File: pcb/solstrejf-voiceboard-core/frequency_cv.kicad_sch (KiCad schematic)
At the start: 0 parts

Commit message: Inital draft of the voice board power supplys and core.
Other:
- title: (none) -> Frequency Control Voltage Summing Amplifier
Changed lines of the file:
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@@
 	(generator_version "8.0")
 	(paper "A4")
+	(title_block
+		(title "Frequency Control Voltage Summing Amplifier")
+		(date "2024-08-24")
+		(rev "1.0")
+	)
 )

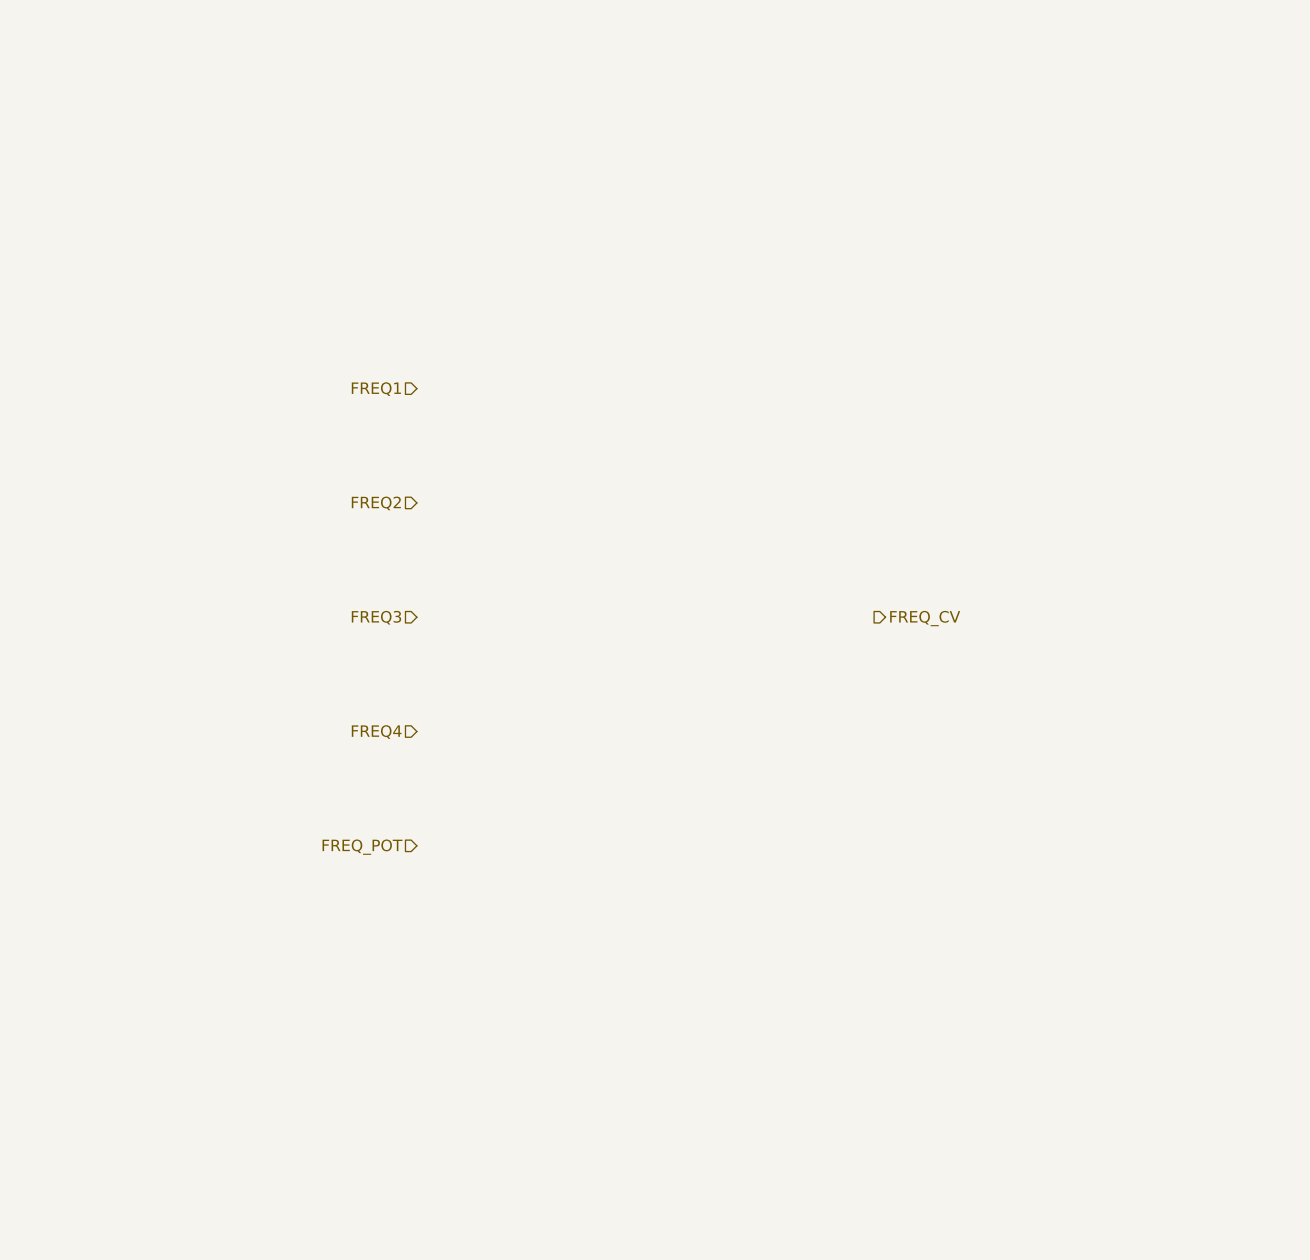
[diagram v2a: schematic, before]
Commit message: created schematic for CV circuits: PAN, VCA, and FREQ. Created a new symbol for the ONESHOT envelope generator
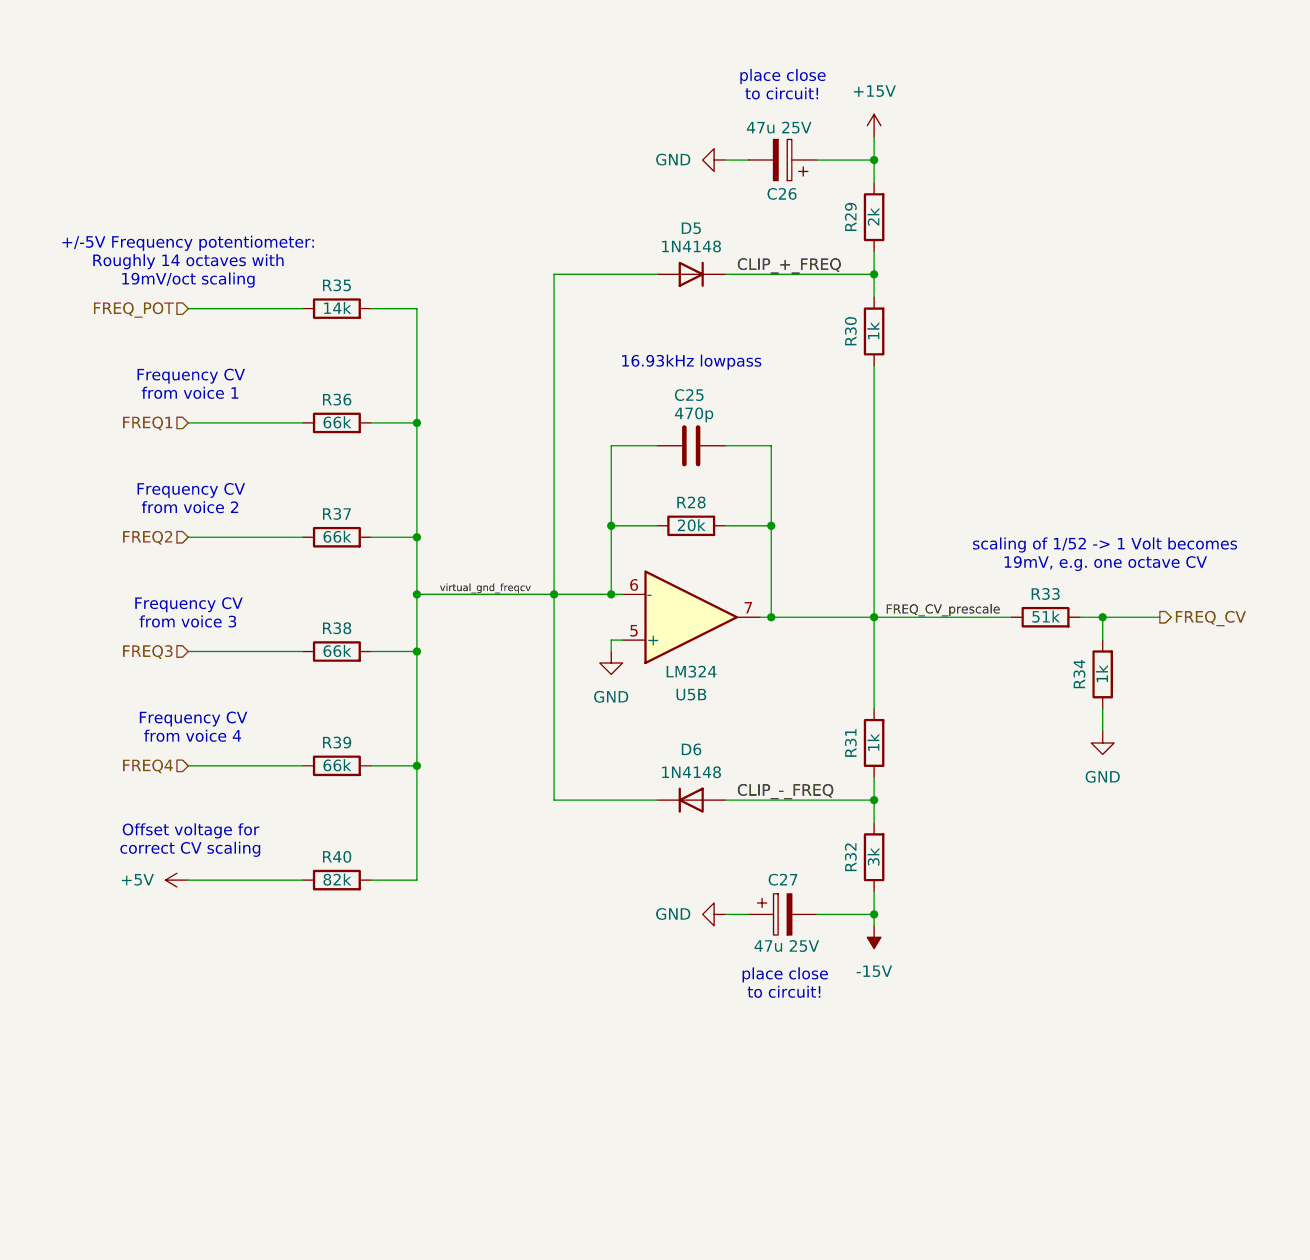
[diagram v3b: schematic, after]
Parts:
- added C25: 470p, Capacitor_THT:C_Disc_D5.0mm_W2.5mm_P5.00mm, symbol Device:C
- added C26, C27: 47u 25V, Capacitor_THT:CP_Radial_D5.0mm_P2.50mm, symbol Device:C_Polarized
- added D5, D6: 1N4148, Diode_THT:D_DO-35_SOD27_P7.62mm_Horizontal, symbol Diode:1N4148
- added R28: 20k, Resistor_THT:R_Axial_DIN0207_L6.3mm_D2.5mm_P10.16mm_Horizontal, symbol Device:R
- added R29: 2k, Resistor_THT:R_Axial_DIN0207_L6.3mm_D2.5mm_P10.16mm_Horizontal, symbol Device:R
- added R30, R31, R34: 1k, Resistor_THT:R_Axial_DIN0207_L6.3mm_D2.5mm_P10.16mm_Horizontal, symbol Device:R
- added R32: 3k, Resistor_THT:R_Axial_DIN0207_L6.3mm_D2.5mm_P10.16mm_Horizontal, symbol Device:R
- added R33: 51k, Resistor_THT:R_Axial_DIN0207_L6.3mm_D2.5mm_P10.16mm_Horizontal, symbol Device:R
- added R35: 14k, Resistor_THT:R_Axial_DIN0207_L6.3mm_D2.5mm_P10.16mm_Horizontal, symbol Device:R
- added R36, R37, R38, R39: 66k, Resistor_THT:R_Axial_DIN0207_L6.3mm_D2.5mm_P10.16mm_Horizontal, symbol Device:R
- added R40: 82k, Resistor_THT:R_Axial_DIN0207_L6.3mm_D2.5mm_P10.16mm_Horizontal, symbol Device:R
- added U5: LM324, Package_DIP:DIP-14_W7.62mm, symbol Amplifier_Operational:LM324
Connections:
- net FREQ1: now also R36.1
- net FREQ2: now also R37.1
- net FREQ3: now also R38.1
- net FREQ4: now also R39.1
- net FREQ_CV: now also R33.2, R34.2
- net FREQ_POT: now also R35.1
- new net +15V: C26.1, R29.2
- new net +5V: R40.1
- new net -15V: C27.2, R32.1
- new net CLIP_+_FREQ: D5.1 (K), R29.1, R30.2
- new net CLIP_-_FREQ: D6.2 (A), R31.1, R32.2
- new net FREQ_CV_prescale: C25.2, R28.2, R30.1, R31.2, R33.1, U5.7
- new net GND: C26.2, C27.1, R34.1, U5.5 (+)
- new net virtual_gnd_freqcv: C25.1, D5.2 (A), D6.1 (K), R28.1, R35.2, R36.2, R37.2, R38.2, R39.2, R40.2, U5.6 (-)
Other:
- note added: "+/-5V Frequency potentiometer: Roughly 14 octaves with 19mV/oct scaling"
- note added: "16.93kHz lowpass"
- note added: "Frequency CV from voice 1"
- note added: "Frequency CV from voice 2"
- note added: "Frequency CV from voice 3"
- note added: "Frequency CV from voice 4"
- note added: "Offset voltage for correct CV scaling"
- note added: "place close to circuit!"
- note added: "scaling of 1/52 -> 1 Volt becomes 19mV, e.g. one octave CV"

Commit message: Updated frequency CV summer circuit to use +/-12V local regulator instead of +/15V. Updated LTspice, notebooks, and KiCad project
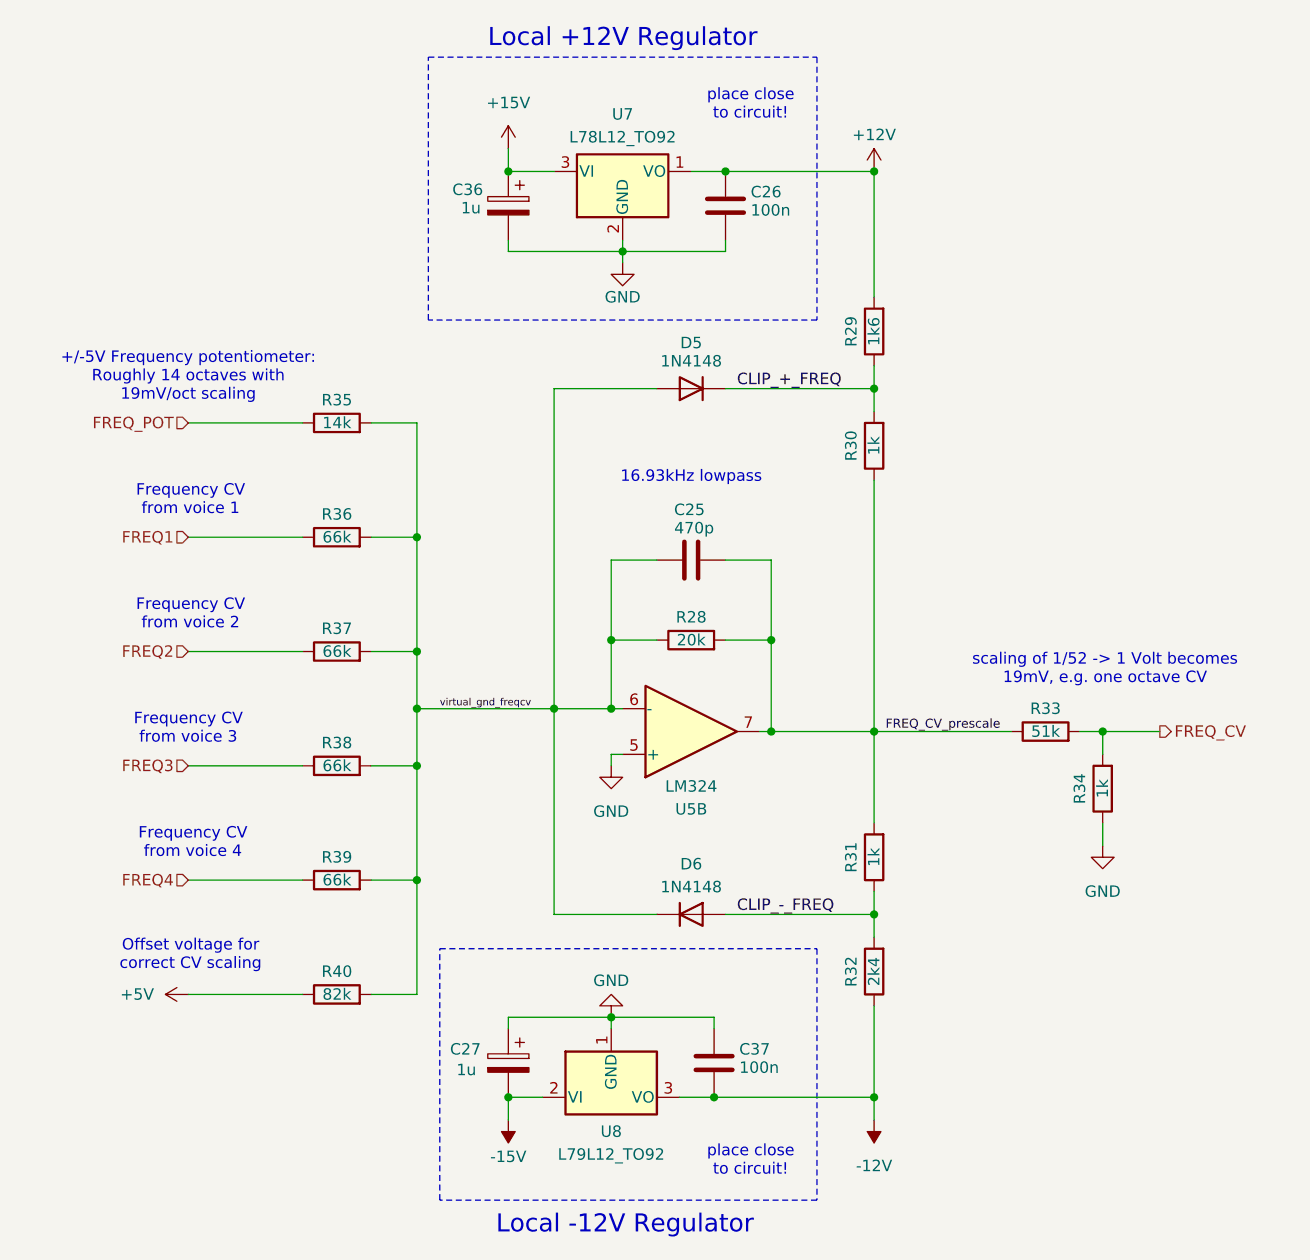
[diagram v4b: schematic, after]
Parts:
- removed C26: 47u 25V, Capacitor_THT:CP_Radial_D5.0mm_P2.50mm, symbol Device:C_Polarized
- added C26, C37: 100n, Capacitor_THT:C_Disc_D5.0mm_W2.5mm_P5.00mm, symbol Device:C
- added C36: 1u, Capacitor_THT:CP_Radial_D5.0mm_P2.50mm, symbol Device:C_Polarized
- added U7: L78L12_TO92, Package_TO_SOT_THT:TO-92_Inline, symbol Regulator_Linear:L78L12_TO92
- added U8: L79L12_TO92, Package_TO_SOT_THT:TO-92_Inline, symbol Regulator_Linear:L79L12_TO92
- C27: value 47u 25V -> 1u
- R29: value 2k -> 1k6
- R32: value 3k -> 2k4
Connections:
- net +15V: now also C36.1, U7.3 (VI); no longer R29.2
- net -15V: now also U8.2 (VI); no longer R32.1
- net GND: now also C26.1, C36.2, C37.2, U7.2 (GND), U8.1 (GND)
- new net +12V: C26.2, R29.2, U7.1 (VO)
- new net -12V: C37.1, R32.1, U8.3 (VO)
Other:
- note added: "Local +12V Regulator"
- note added: "Local -12V Regulator"
- moved on the sheet: C25, C27, D5, D6, R28, R29, R30, R31, R32, R33, R34, R35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

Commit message: Finish layout of the voice board. Included 3D renders in README.
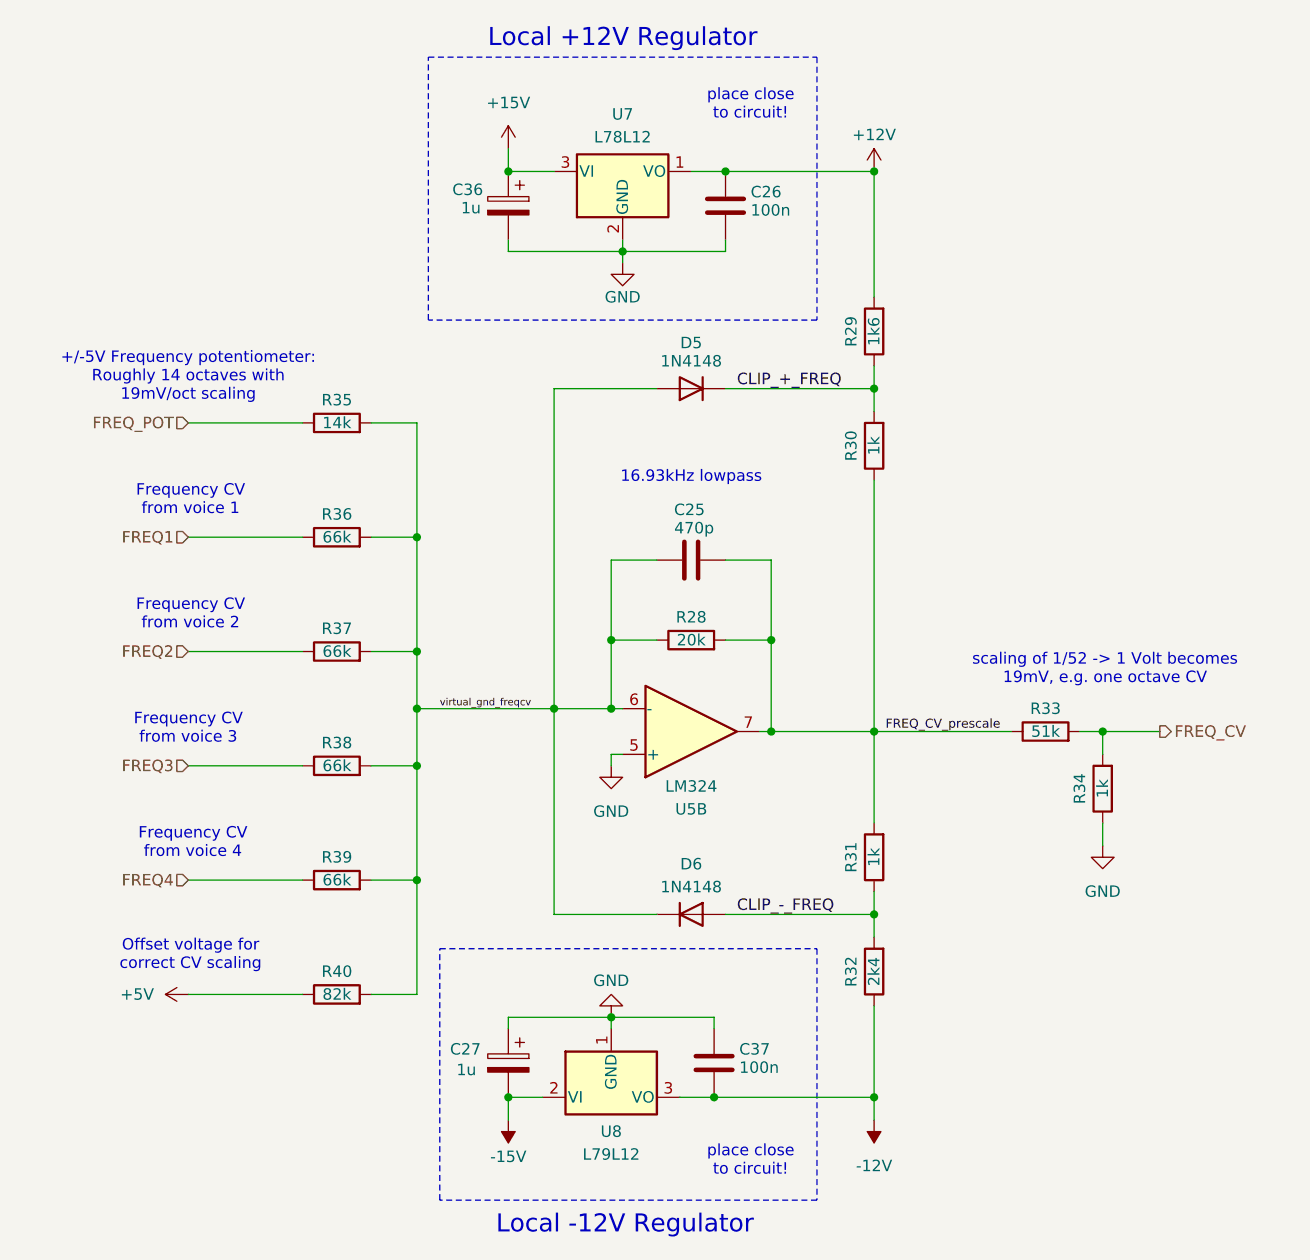
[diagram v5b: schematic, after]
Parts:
- U7: value L78L12_TO92 -> L78L12
- U8: value L79L12_TO92 -> L79L12
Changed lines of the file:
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@@
 			)
 		)
-		(property "Value" "L79L12_TO92"
+		(property "Value" "L79L12"
 			(at 123.19 148.59 0)
 			(effects
@@
 			)
 		)
-		(property "Value" "L78L12_TO92"
+		(property "Value" "L78L12"
 			(at 124.46 35.56 0)
 			(effects
